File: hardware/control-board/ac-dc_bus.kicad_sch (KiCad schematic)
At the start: 26 parts, among them K1 Relay_SPDT, K2 Relay_SPDT, Q1 NMOS, U1 ACS773LCB-050B-PFF, U2 OPA365xxD

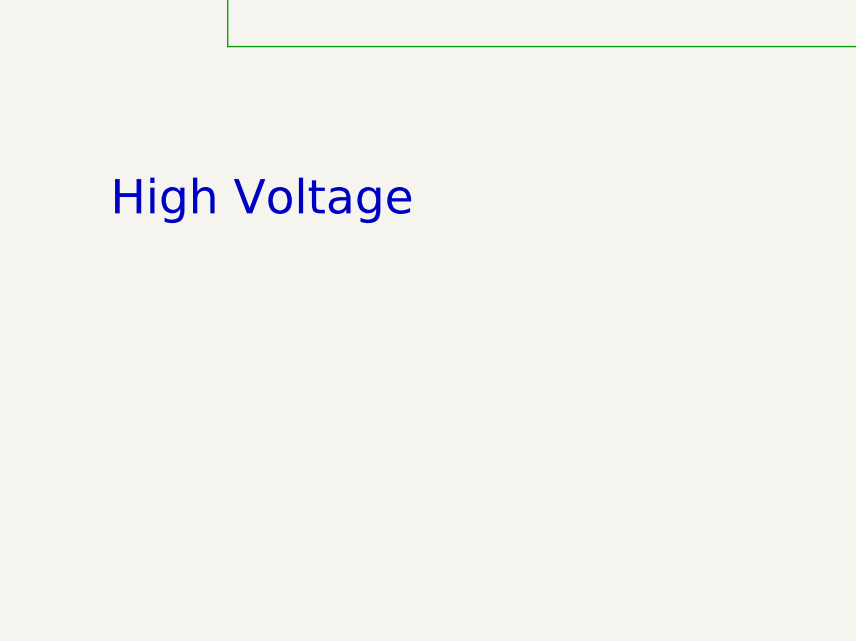
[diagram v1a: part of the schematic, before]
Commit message: added titles to sheets
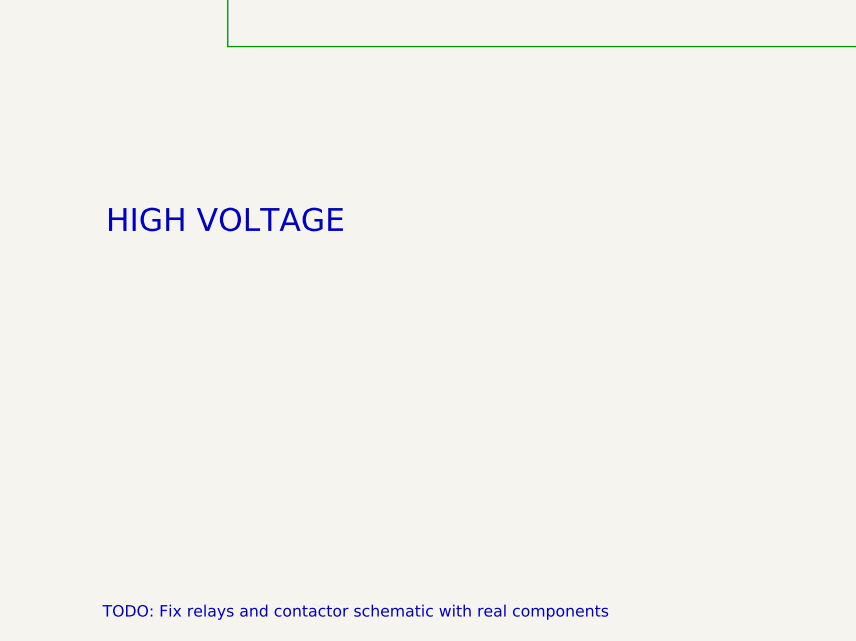
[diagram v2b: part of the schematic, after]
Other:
- note added: "HIGH VOLTAGE"
- note added: "TODO: Fix relays and contactor schematic with real components"
- note removed: "High Voltage"
- title: (none) -> AC-DC Bus
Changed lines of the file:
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@@
 	(generator_version "9.0")
 	(paper "A4")
+	(title_block
+		(title "AC-DC Bus")
+	)
 	(text "Normally open relay when closed \nbypasses soft start resistor"
 		(exclude_from_sim no)
@@
 			(font
 				(size 1.27 1.27)
-			)
-		)
-	)
-	(text "High Voltage"
-		(exclude_from_sim no)
-		(at 45.72 141.478 0)
-		(effects
-			(font
-				(size 3.81 3.81)
 			)
 		)
@@
 			)
 		)
+	)
+	(text "TODO: Fix relays and contactor schematic with real components"
+		(exclude_from_sim no)
+		(at 56.134 187.452 0)
+		(effects
+			(font
+				(size 1.27 1.27)
+			)
+		)
+	)
+	(text "HIGH VOLTAGE"
+		(exclude_from_sim no)
+		(at 41.656 144.018 0)
+		(effects
+			(font
+				(size 2.54 2.54)
+			)
+		)

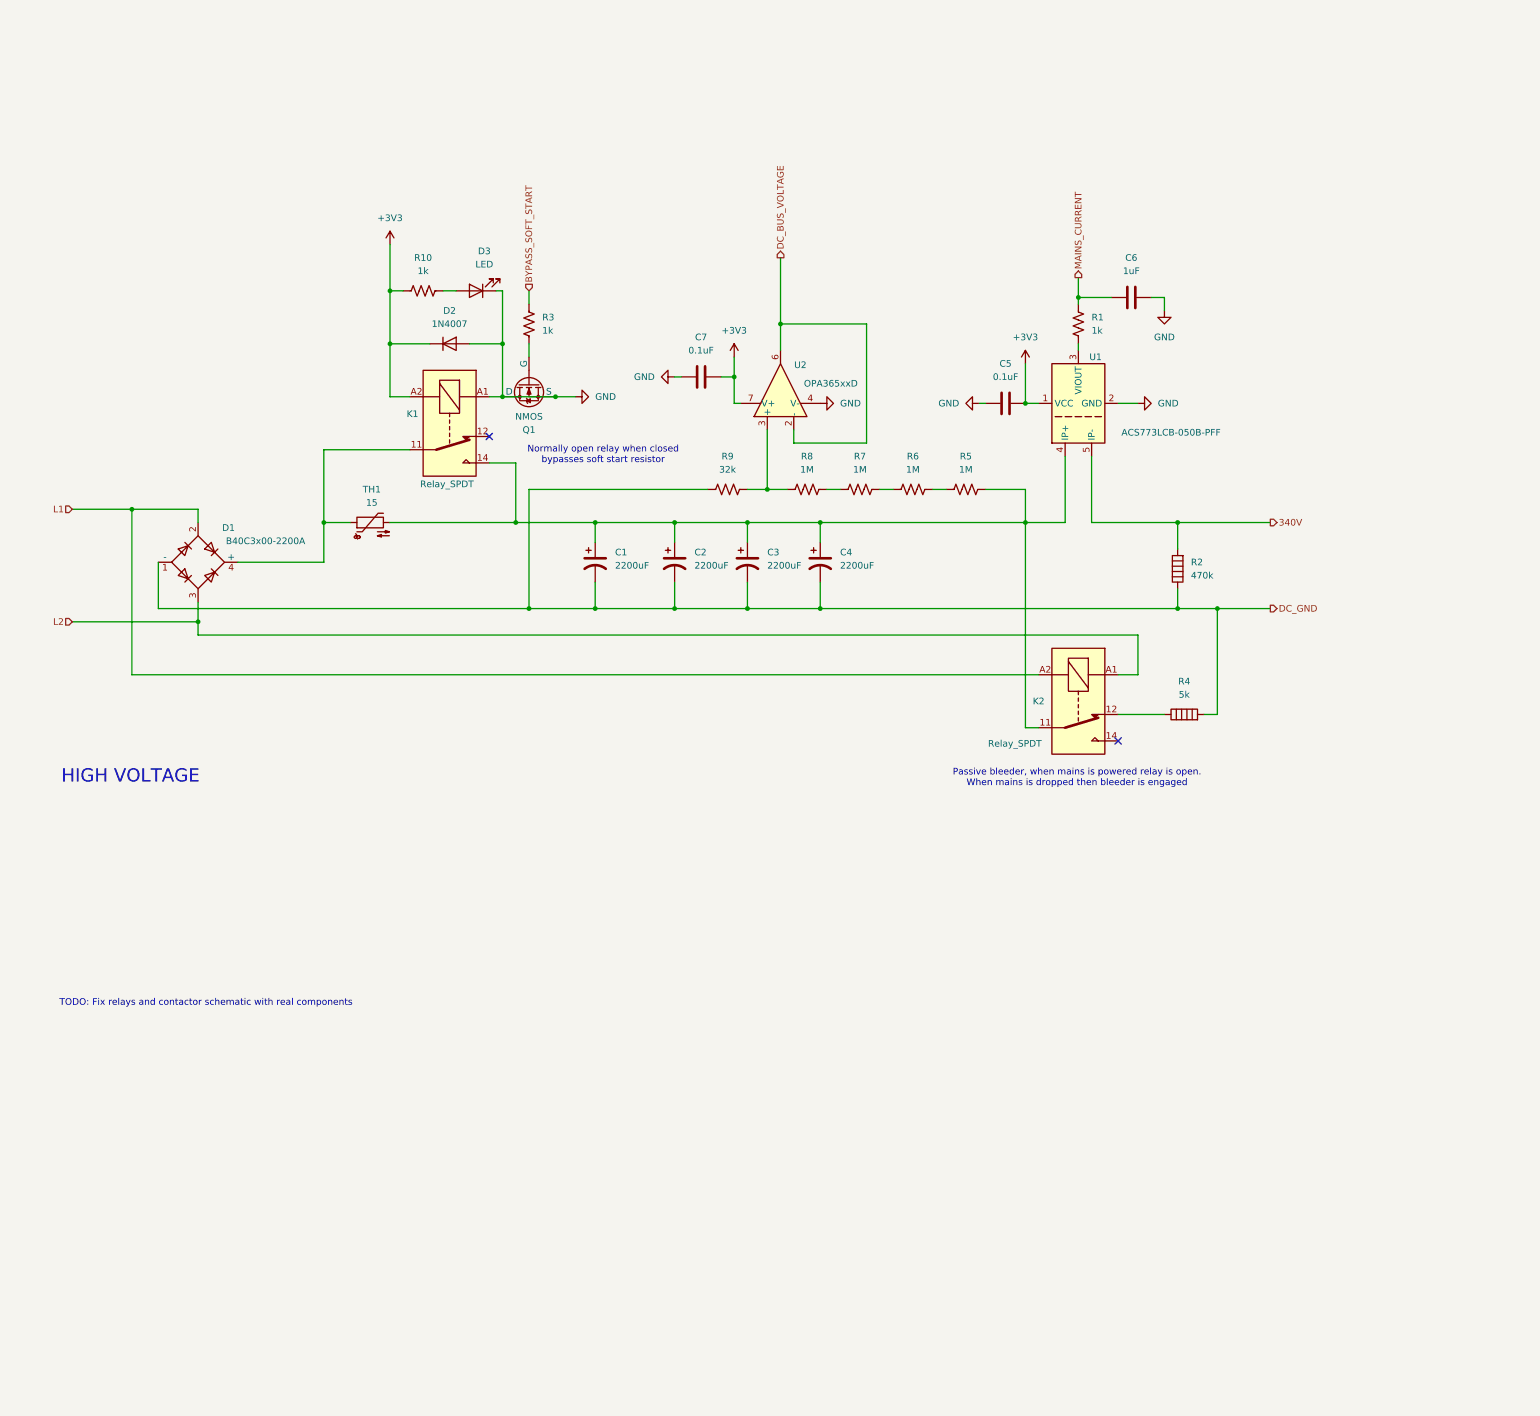
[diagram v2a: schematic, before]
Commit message: removed opamp, will replace with isolated opamp
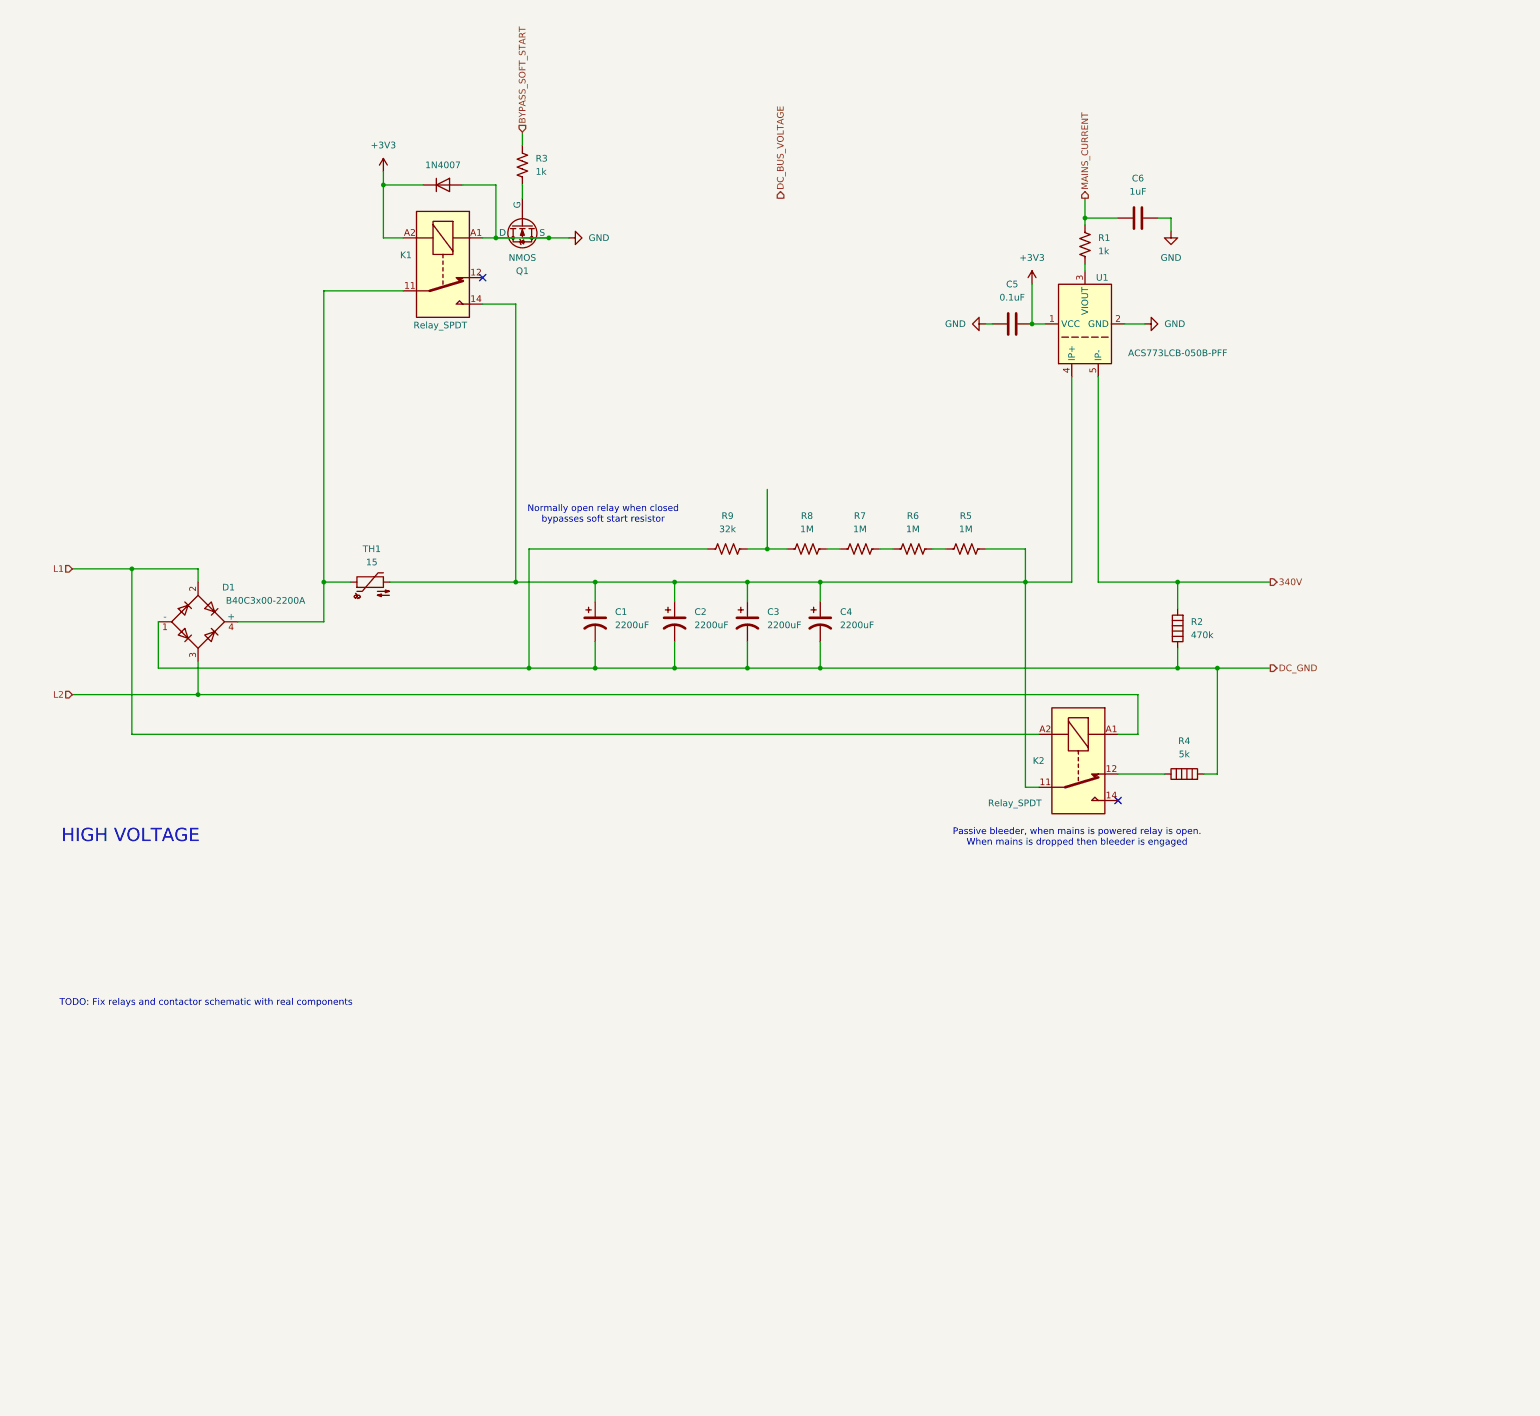
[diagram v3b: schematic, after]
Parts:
- removed C7: 0.1uF, symbol Device:C
- removed D3: LED, symbol Device:LED
- removed R10: 1k, symbol Device:R_US
- removed U2: OPA365xxD, Package_SO:SOIC-8_3.9x4.9mm_P1.27mm, symbol Amplifier_Operational:OPA365xxD
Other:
- moved on the sheet: C1, C2, C3, C4, C5, C6, D1, K1, K2, Q1, R1, R2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

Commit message: final draft of ac-dc done
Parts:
- added 1k: R_US, symbol Device:R_US
- added C10, C7, C9: C, symbol Device:C
- added C11, C12, C13, C15: 0.1uF, symbol Device:C
- added C14: 0.1uf, symbol Device:C
- added R10, R11, R13, R14: 1k, symbol Device:R_US
- added U2: TLV9001IDCK, Package_TO_SOT_SMD:SOT-353_SC-70-5, symbol Amplifier_Operational:TLV9001IDCK
- added U?: AMC3311, Package_SO:SOIC-16W_7.5x10.3mm_P1.27mm, symbol isolated_opamp:AMC3311
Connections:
- net +3V3: now also C11.1, C12.1, C14.1, R10.2, U2.5 (V+), U?.12 (VDD), U?.13 (LDO_OUT), U?.16 (DCDC_IN)
- net DC_BUS_VOLTAGE: now also C13.1, R13.2, U2.4
- net GND: now also C11.2, C12.2, C14.2, C15.2, R14.2, U?.15 (DCDC_GND), U?.9 (GND)
- net at C1.1, C2.1, C3.1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: now also R5.1; no longer K2.11, R5.2
- net at R8.1: now also R7.2; no longer R9.2
- net at R8.2: now also R9.1, C10.1, U?.6 (INP); no longer R7.1
- net at R6.2: now also R7.1; no longer R5.1
- net at R6.1: now also R5.2; no longer R7.2
- net 340V renamed VDC
- net VDC: now also K2.11
- net DC_GND renamed GNDPWR
- net GNDPWR: now also R9.2, C10.2, C7.2, C9.2, U?.2 (DCDC_HGND), U?.7 (INN), U?.8 (HGND); no longer R9.1
- new net: C15.1, R11.2, R14.1, U2.1 (+)
- new net: C9.1, U?.1 (DCDC_OUT), U?.3 (HLDO_IN)
- new net: 1k.2, U2.3 (-)
- new net: C7.1, U?.5 (HLDO_OUT)
- new net: C13.2, R13.1, U2.2 (V-)
- new net DC_BUS_VOLTAGE_VALID: R10.1, U?.14 (DIAG)
- new net OUTN: 1k.1, U?.10 (OUTN)
- new net OUTP: R11.1, U?.11 (OUTP)
- no-connect marks 2 -> 3
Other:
- note added: "High Voltage DC Bus Measurment"
- moved on the sheet: C1, C2, C3, C4, C5, C6, D1, K1, K2, Q1, R1, R2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

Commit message: mcu controller added
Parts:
- gave numbers to parts that had none: 1
- renumbered 1k to 1k1
